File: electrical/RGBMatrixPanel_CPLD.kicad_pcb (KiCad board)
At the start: 2 copper layers, 71.1 x 59.7 mm, 41 parts, among them J1 BARREL_JACK, J2 CONN_01X01, J3 CONN_01X01, J4 CONN_01X01, J5 CONN_01X01, J6 CONN_01X06, J7 CONN_02X08, J8 CONN_01X06, J9 CONN_01X03, Q1 Photo_Trans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

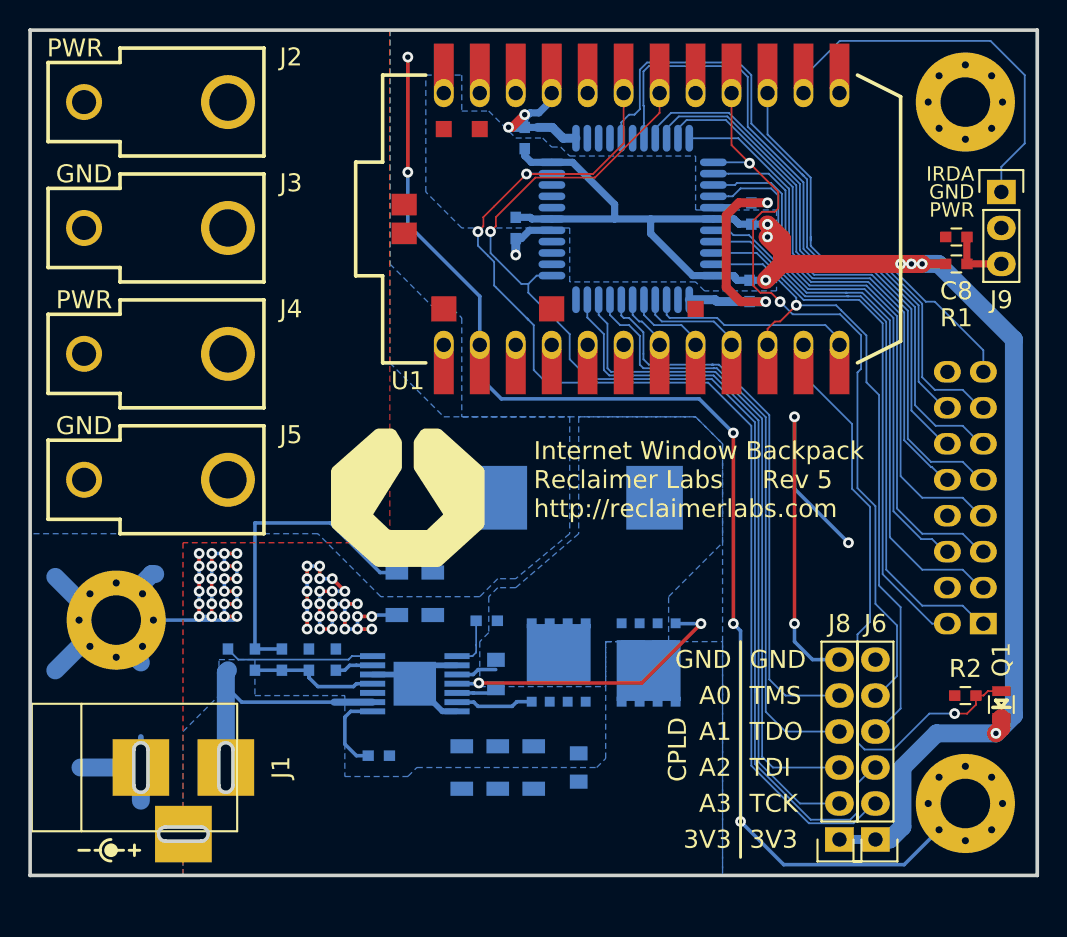
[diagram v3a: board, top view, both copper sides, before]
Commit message: Added buck converter
Added an on-board 24V to 5V buck converter to lower the current going
through the connector to a safe level. Now the magic smoke stays safely
contained.
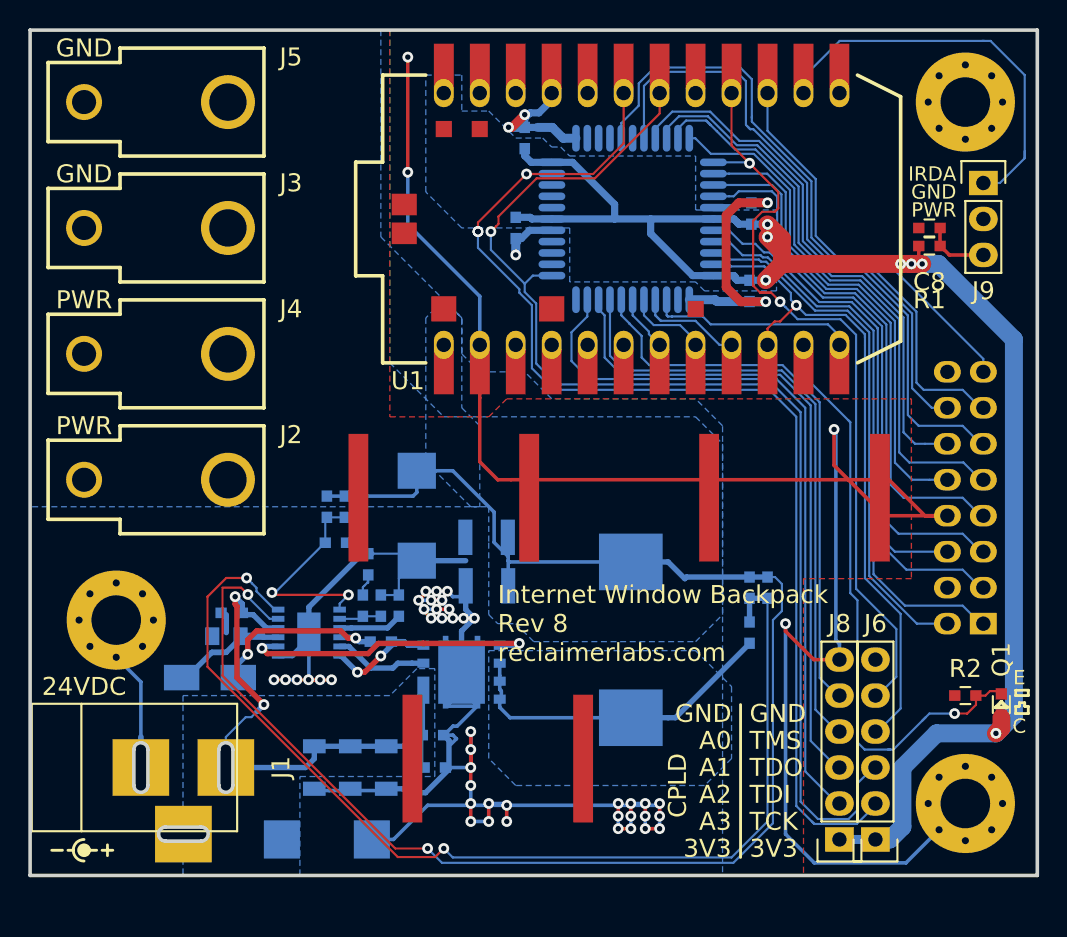
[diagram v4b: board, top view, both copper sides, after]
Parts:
- removed G***: LOGO, Reclaimer_Labs:Reclaimer_Labs2
- removed Q2: CSD17307Q5A, Reclaimer_Labs:MOSFET_Q5A
- removed Q3: CSD18531Q5A, Reclaimer_Labs:MOSFET_Q5A
- added C16: 2200pF, Capacitors_SMD:C_0603, B.Cu at (74.3, 97.8)
- added C17: 1uF, Capacitors_SMD:C_0603, B.Cu at (65.0, 98.3)
- added C18: 0.1uF, Capacitors_SMD:C_0603, B.Cu at (102.9, 96.5)
- added C19: 0.1uF, Capacitors_SMD:C_0603, B.Cu at (76.8, 97.8)
- added C20: 100pF, Capacitors_SMD:C_0603, B.Cu at (75.6, 97.8)
- added C21: DNP, Capacitors_SMD:C_0603, B.Cu at (71.8, 90.8)
- added C22: 100uF, Capacitors_Tantalum_SMD:CP_Tantalum_Case-D_EIA-7343-31_Reflow, B.Cu at (78.1, 91.4)
- added D1: B140, Diodes_SMD:D_SMA_Standard, B.Cu at (63.5, 102.9)
- added R14: 7k32, Capacitors_SMD:C_0603, B.Cu at (101.6, 99.7)
- added R7: 28k0, Capacitors_SMD:C_0603, B.Cu at (101.6, 96.5)
- added U4: CSD87351Q5D, Reclaimer_Labs:CSD87351Q5D, B.Cu at (81.3, 102.5)
- added X4: HEATSiNK, Reclaimer_Labs:573100D00010G, F.Cu at (83.8, 108.6)
- added X5: HEATSiNK, Reclaimer_Labs:573100D00010G, F.Cu at (104.8, 90.2)
- added X6: HEATSiNK, Reclaimer_Labs:573100D00010G, F.Cu at (80.0, 90.2)
- C1, C2, C3: value 4.7uF -> 10uF
- C11: value 0.47uF -> DNP; footprint Capacitors_SMD:C_0805 -> Capacitors_Tantalum_SMD:CP_Tantalum_Case-D_EIA-7343-31_Reflow
- C12: value 1.0uF -> 10uF; footprint Capacitors_SMD:C_0603 -> Capacitors_SMD:C_0805
- C13: value 390pF -> 1uF
- C14: footprint Capacitors_SMD:C_1206 -> Capacitors_SMD:C_1210
- C15: value DNP -> 100uF; footprint Capacitors_SMD:C_1206 -> Capacitors_SMD:C_1210
- C4: footprint Capacitors_SMD:C_0805 -> Capacitors_SMD:C_0603
- C5: value 0.01uF -> 1uF
- L1: value 2.2uH -> 1.5uH
- Q1: footprint Reclaimer_Labs:Photo_Trans_0805 -> Reclaimer_Labs:Photo_Trans_ALS-PT19-315C
- R3: value 73k2 -> 10k
- R4: value 1k69 -> 100k
- R5: value 73k2 -> 100k
- U3: value LM3150 -> LTC3854; footprint Reclaimer_Labs:TSSOP-14-0.65mm-EP -> Reclaimer_Labs:12-MSE
- moved J2 26.7 mm to (59.7, 88.9)
- moved J5 26.7 mm to (59.7, 62.2)
- moved C11 16.7 mm to (71.8, 114.3), turned to 0 degrees
- moved C3 15.5 mm to (70.9, 109.2), turned to 270 degrees
- moved C12 13.7 mm to (64.7, 99.9), turned to 180 degrees
- moved R4 12.9 mm to (73.0, 90.8), turned to 90 degrees
- moved R5 12.2 mm to (74.3, 90.8), turned to 90 degrees
- moved R3 12.0 mm to (74.7, 94.9)
- moved L1 10.7 mm to (93.2, 100.2), turned to 90 degrees
- moved C4 10.5 mm to (79.2, 106.9), turned to 0 degrees
- moved C2 10.4 mm to (73.4, 109.2), turned to 270 degrees
- moved C5 10.3 mm to (79.4, 109.2), turned to 0 degrees
- moved C13 8.98 mm to (75.6, 100.3), turned to 180 degrees
- moved R6 8.47 mm to (72.4, 93.3), turned to 180 degrees
- moved U3 8.30 mm to (70.5, 99.7), turned to 270 degrees
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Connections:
- C11 pad 1: /BST -> VIN
- C11 pad 2: /SW -> GND
- C12 pad 1: /VCC -> /INTVCC
- C13 pad 1: +5V -> /SW
- C13 pad 2: /FB -> Net-(C13-Pad2)
- C5 pad 1: /SS -> VIN
- L1 pad 1: /SW -> Net-(L1-Pad1)
- R3 pad 1: VIN -> Net-(C16-Pad2)
- R3 pad 2: /RON -> GND
- R4 pad 1: /SW -> /FB
- R4 pad 2: /ILIM -> +5V
- R5 pad 1: +5V -> /FB
- R5 pad 2: /FB -> +5V
- R6 pad 1: /FB -> GND
- R6 pad 2: GND -> /FB
- U3 pad 1: /VCC -> /FB
- U3 pad 10: /SW -> VIN
- U3 pad 11: /HG -> +5V
- U3 pad 12: /BST -> /SENSE+
- U3 pad 13: /LG -> GND
- U3 pad 2: VIN -> /ITH
- U3 pad 3: Net-(U3-Pad3) -> /SS
- U3 pad 4: /FB -> Net-(C13-Pad2)
- U3 pad 5: GND -> /DRVH
- U3 pad 6: /SS -> /SW
- U3 pad 7: /RON -> GND
- U3 pad 8: /ILIM -> /DRVL
- U3 pad 9: GND -> /INTVCC
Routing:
- net +5V: track 24.2 -> 117.1 mm, vias 0 -> 2
- net /SENSE+: track 0.00 -> 76.9 mm, vias 0 -> 2
- net GND: track 254.1 -> 302.4 mm, vias 63 -> 51
- net /DRVL: track 0.00 -> 28.1 mm, vias 0 -> 2
- net Net-(L1-Pad1): track 0.00 -> 23.3 mm
- net /HG: track 20.8 -> 0.00 mm, vias 2 -> 0
- net VIN: track 18.8 -> 39.3 mm, vias 0 -> 2
- net Net-(C13-Pad2): track 0.00 -> 13.3 mm, vias 0 -> 2
- net /RON: track 10.6 -> 0.00 mm
- net /INTVCC: track 0.00 -> 9.02 mm
- net /FB: track 9.18 -> 16.4 mm, vias 0 -> 2
- net /DRVH: track 0.00 -> 6.69 mm
- net /VCC: track 6.02 -> 0.00 mm
- net /LG: track 5.54 -> 0.00 mm
- net /SW: track 2.88 -> 7.99 mm, vias 0 -> 2
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- added copper zone on B.Cu, net Net-(L1-Pad1)
- removed copper zone on B.Cu, net /SW
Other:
- net class Default: clearance 0.12446 -> 0.14986; trace_width 0.127 -> 0.1524
- net class Power: clearance 0.12446 -> 0.14986
- rule trace_clearance: 0.12446 -> 0.14986
- rule trace_min: 0.12446 -> 0.14986
- board text added: "24VDC"
- board text added: "C"
- board text added: "E"
- board text added: "Internet Window Backpack Rev 8 reclaimerlabs.com"
- board text removed: "Internet Window Backpack Reclaimer Labs Rev 5 http://reclaimerlabs.com"
